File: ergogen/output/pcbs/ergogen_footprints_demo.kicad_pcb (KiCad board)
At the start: 2 copper layers, 95 x 95 mm, 53 parts

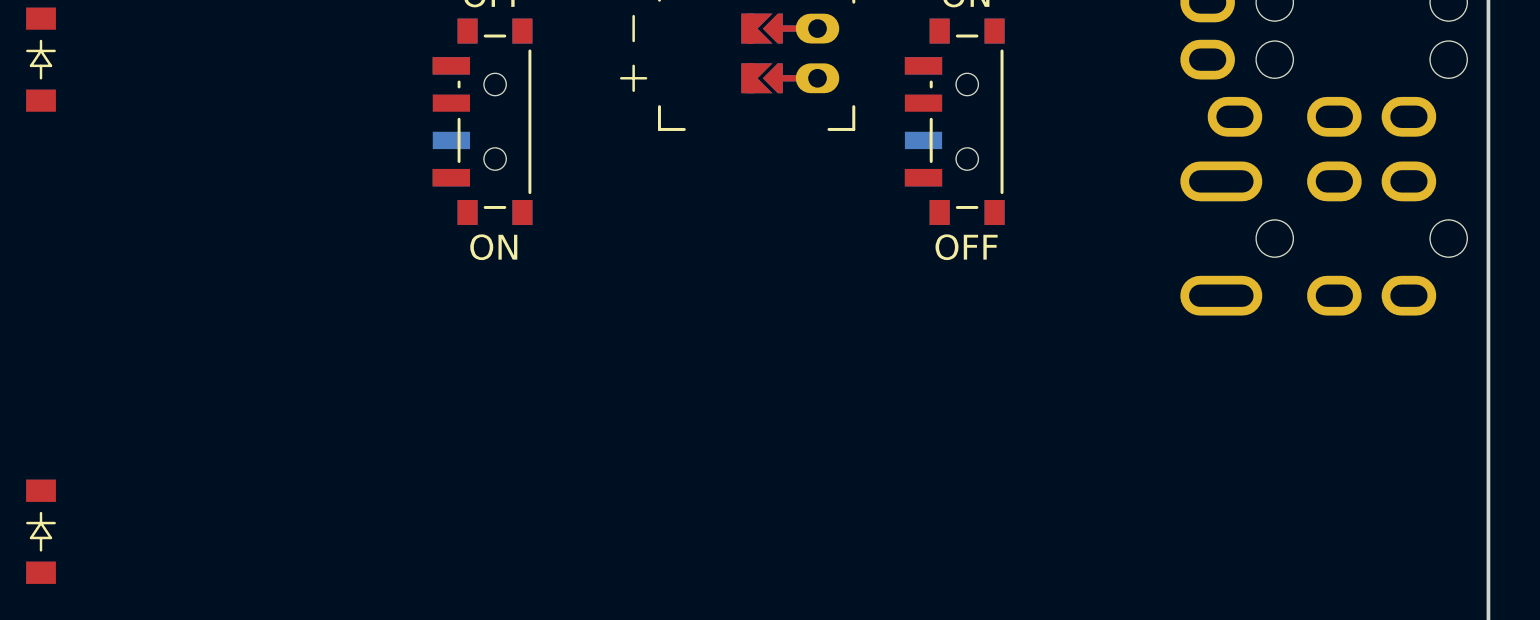
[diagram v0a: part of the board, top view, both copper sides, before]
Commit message: Add SSD1306 footprint
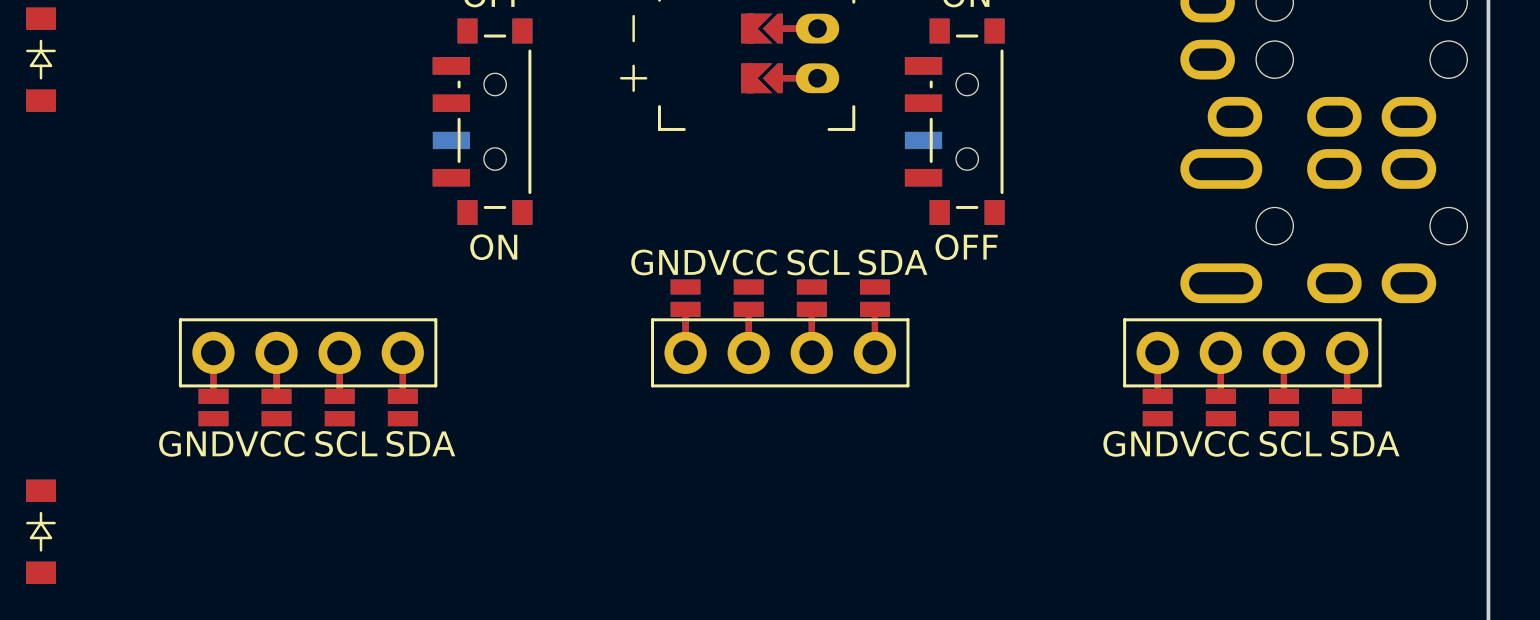
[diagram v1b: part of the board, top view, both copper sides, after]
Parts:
- added DISP4: , ceoloide:display_ssd1306, F.Cu at (138.0, 127.5)
- added DISP5: , ceoloide:display_ssd1306, F.Cu at (119.0, 127.5)
- added DISP6: , ceoloide:display_ssd1306, F.Cu at (100.0, 127.5)
- moved TRRS2 0.50 mm to (147.5, 108.0)
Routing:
- net VCC: track 7.51 -> 18.0 mm
- net SDA: track 10.5 -> 21.0 mm
- net SCL: track 10.5 -> 21.0 mm
- net GND: track 54.2 -> 64.7 mm

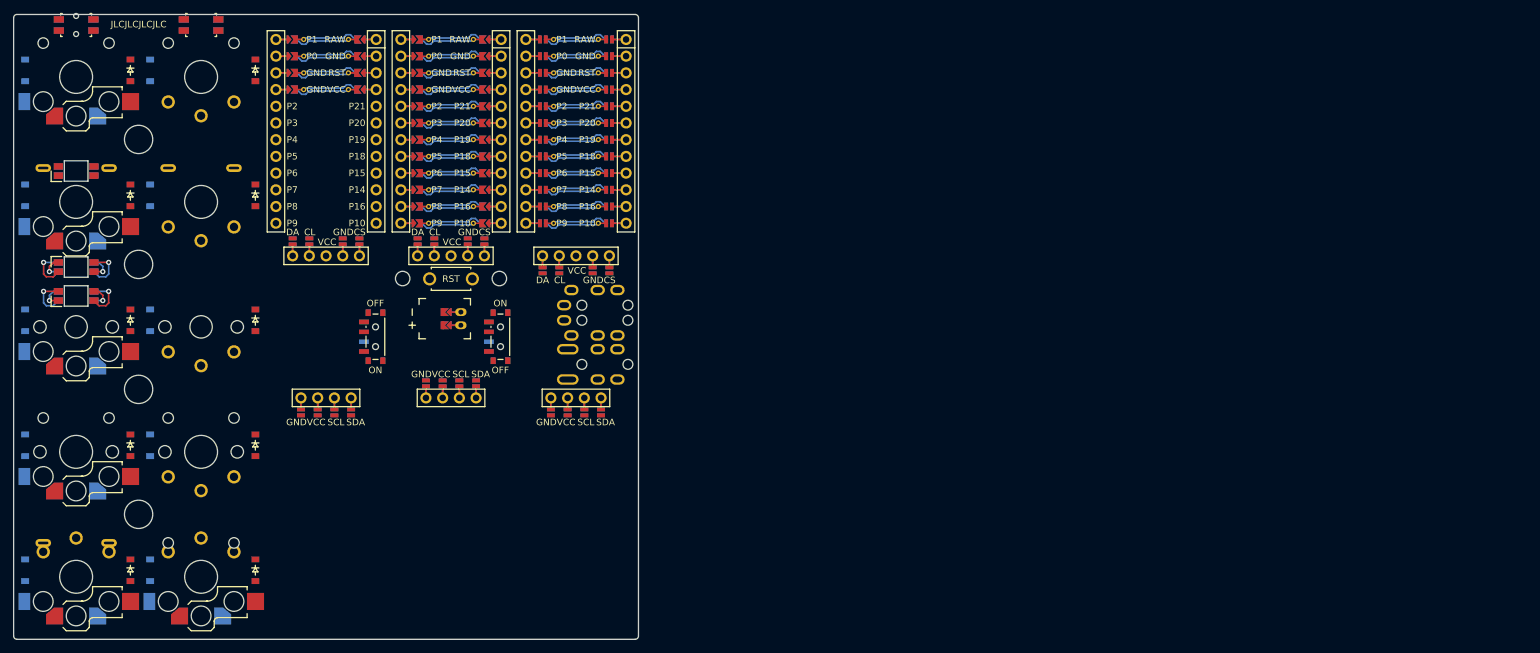
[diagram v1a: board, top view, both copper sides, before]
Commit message: Add mirror options to test footprints
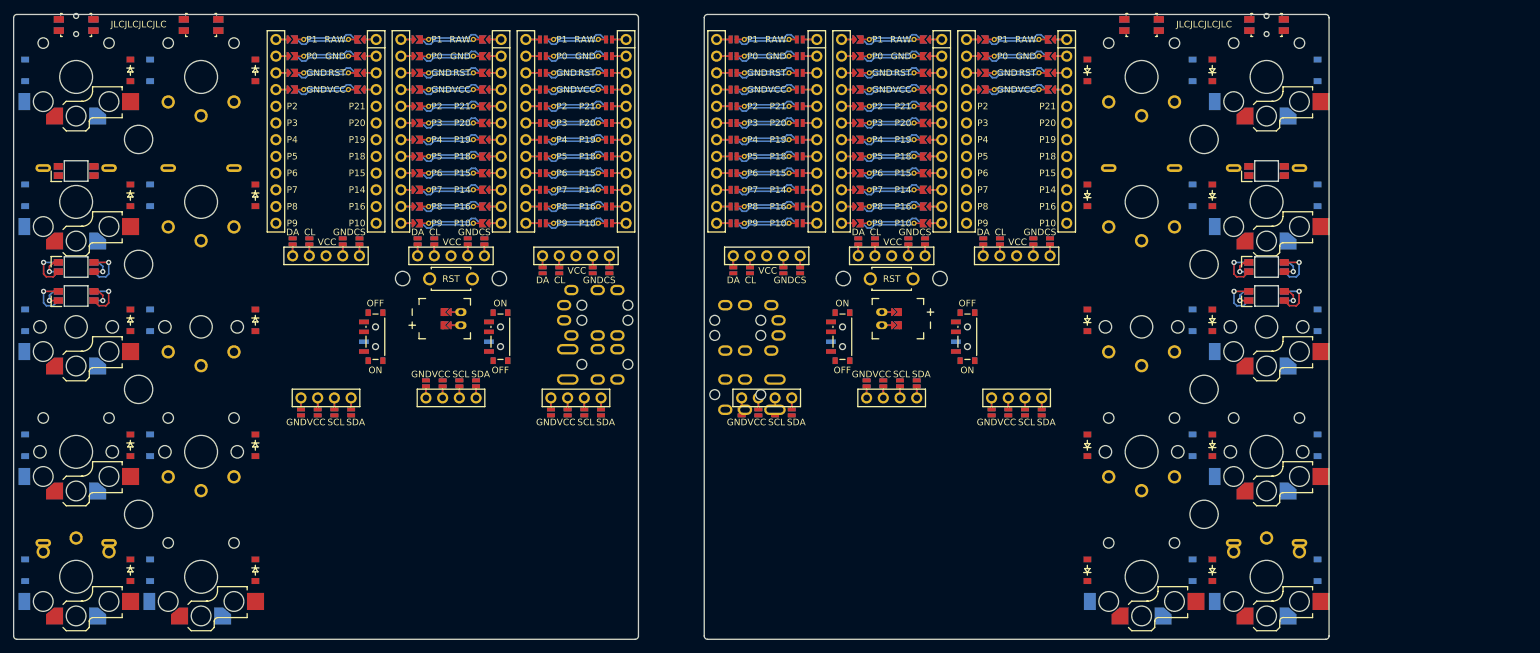
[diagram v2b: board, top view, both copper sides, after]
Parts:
- added D21: , ceoloide:diode_tht_sod123, F.Cu at (70.2, 137.0)
- added D22: , ceoloide:diode_tht_sod123, F.Cu at (70.2, 118.0)
- added D23: , ceoloide:diode_tht_sod123, F.Cu at (70.2, 99.0)
- added D24: , ceoloide:diode_tht_sod123, F.Cu at (70.2, 80.0)
- added D25: , ceoloide:diode_tht_sod123, F.Cu at (70.2, 61.0)
- added D26: , ceoloide:diode_tht_sod123, F.Cu at (89.2, 137.0)
- added D27: , ceoloide:diode_tht_sod123, F.Cu at (89.2, 118.0)
- added D28: , ceoloide:diode_tht_sod123, F.Cu at (89.2, 99.0)
- added D29: , ceoloide:diode_tht_sod123, F.Cu at (89.2, 80.0)
- added D30: , ceoloide:diode_tht_sod123, F.Cu at (89.2, 61.0)
- added D31: , ceoloide:diode_tht_sod123, F.Cu at (234.8, 137.0)
- added D32: , ceoloide:diode_tht_sod123, F.Cu at (234.8, 118.0)
- added D33: , ceoloide:diode_tht_sod123, F.Cu at (234.8, 99.0)
- added D34: , ceoloide:diode_tht_sod123, F.Cu at (234.8, 80.0)
- added D35: , ceoloide:diode_tht_sod123, F.Cu at (234.8, 61.0)
- added D36: , ceoloide:diode_tht_sod123, F.Cu at (215.8, 137.0)
- added D37: , ceoloide:diode_tht_sod123, F.Cu at (215.8, 118.0)
- added D38: , ceoloide:diode_tht_sod123, F.Cu at (215.8, 99.0)
- added D39: , ceoloide:diode_tht_sod123, F.Cu at (215.8, 80.0)
- added D40: , ceoloide:diode_tht_sod123, F.Cu at (215.8, 61.0)
- added DISP10: , ceoloide:display_ssd1306, F.Cu at (186.0, 127.5)
- added DISP11: , ceoloide:display_ssd1306, F.Cu at (100.0, 127.5)
- added DISP12: , ceoloide:display_ssd1306, F.Cu at (205.0, 127.5)
- added DISP7: , ceoloide:display_ssd1306, F.Cu at (138.0, 127.5)
- added DISP8: , ceoloide:display_ssd1306, F.Cu at (167.0, 127.5)
- added DISP9: , ceoloide:display_ssd1306, F.Cu at (119.0, 127.5)
- added JST2: , ceoloide/battery_connector_jst_ph_2, F.Cu at (184.5, 98.8)
- added LED4: , ceoloide:led_SK6812mini-e (per-key, reversible), B.Cu at (243.0, 95.3)
- added LED5: , ceoloide:led_SK6812mini-e (underglow, reversible), B.Cu at (62.0, 90.9)
- added LED6: , ceoloide:led_SK6812mini-e (underglow, reversible), B.Cu at (243.0, 90.9)
- added MCU4: , ceoloide:nice_nano, F.Cu at (186.0, 69.0)
- added MCU5: , ceoloide:nice_nano, F.Cu at (100.0, 69.0)
- added MCU6: , ceoloide:nice_nano, F.Cu at (205.0, 69.0)
- added MH10: , ceoloide:mounting_hole_npth, F.Cu at (193.3, 92.7)
- added MH11: , ceoloide:mounting_hole_npth, F.Cu at (126.3, 92.7)
- added MH12: , ceoloide:mounting_hole_npth, F.Cu at (178.7, 92.7)
- added MH7: , ceoloide:mounting_hole_npth, F.Cu at (233.5, 90.5)
- added MH8: , ceoloide:mounting_hole_npth, F.Cu at (233.5, 71.5)
- added MH9: , ceoloide:mounting_hole_npth, F.Cu at (111.7, 92.7)
- added PWR3: power_switch, ceoloide:power_switch_smd_side, F.Cu at (107.5, 101.5)
- added PWR4: power_switch, ceoloide:power_switch_smd_side, F.Cu at (197.5, 101.5)
- added RST4: reset_button_smd_side, ceoloide:reset_button_smd_side, F.Cu at (243.0, 54.1)
- added RST5: reset_switch_tht_top, ceoloide:reset_switch_tht_top, F.Cu at (119.0, 92.7)
- added RST6: reset_switch_tht_top, ceoloide:reset_switch_tht_top, F.Cu at (186.0, 92.7)
- added S11: , ceoloide:switch_choc_v1_v2, B.Cu at (81.0, 62.0)
- added S12: , ceoloide:switch_choc_v1_v2, B.Cu at (224.0, 62.0)
- added S13: , ceoloide:switch_choc_v1_v2, B.Cu at (81.0, 81.0)
- added S14: , ceoloide:switch_choc_v1_v2, B.Cu at (224.0, 81.0)
- added S15: , ceoloide:switch_choc_v1_v2, B.Cu at (81.0, 100.0)
- added S16: , ceoloide:switch_choc_v1_v2, B.Cu at (224.0, 100.0)
- added S17: , ceoloide:switch_choc_v1_v2, B.Cu at (81.0, 119.0)
- added S18: , ceoloide:switch_choc_v1_v2, B.Cu at (224.0, 119.0)
- added S19: , ceoloide:switch_choc_v1_v2, B.Cu at (81.0, 138.0)
- added S20: , ceoloide:switch_choc_v1_v2, B.Cu at (224.0, 138.0)
- added TRRS3: TRRS-PJ-320A-dual, ceoloide:trrs_pj320a (reversible, symmetric), F.Cu at (147.5, 108.0)
- added TRRS4: TRRS-PJ-320A-dual, ceoloide:trrs_pj320a (reversible, symmetric), F.Cu at (157.5, 108.0)
- D11, D12, D13, D14, D15, D16, D17, D18, D19, D20: moved to B.Cu
- DISP4, DISP5, DISP6: footprint ceoloide:display_ssd1306 -> ceoloide:nice_view
- LED3: footprint ceoloide:led_SK6812mini-e (underglow, reversible) -> ceoloide:led_SK6812mini-e (per-key, reversible)
- RST3: value reset_switch_tht_top -> reset_button_smd_side; footprint ceoloide:reset_switch_tht_top -> ceoloide:reset_button_smd_side
- TRRS2: footprint ceoloide:trrs_pj320a (reversible, symmetric) -> ceoloide:trrs_pj320a (reversible)
- moved S4 184.9 mm to (243.0, 81.0)
- moved LED2 182.0 mm to (243.0, 76.3)
- moved S2 182.0 mm to (243.0, 62.0)
- moved D11 180.5 mm to (250.8, 137.0), turned to 90 degrees
- moved D12 180.5 mm to (250.8, 118.0), turned to 90 degrees
- moved D13 180.5 mm to (250.8, 99.0), turned to 90 degrees
- moved D14 180.5 mm to (250.8, 80.0), turned to 90 degrees
- moved D15 180.5 mm to (250.8, 61.0), turned to 90 degrees
- moved S6 166.4 mm to (243.0, 100.0)
- moved S8 163.1 mm to (243.0, 119.0)
- moved RST2 162.0 mm to (224.0, 54.1)
- moved S10 162.0 mm to (243.0, 138.0)
- moved D16 142.5 mm to (231.8, 137.0), turned to 90 degrees
- moved D17 142.5 mm to (231.8, 118.0), turned to 90 degrees
- moved D18 142.5 mm to (231.8, 99.0), turned to 90 degrees
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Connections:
- D11 pad 2: c1_r5 -> mirror_c1_r5
- D12 pad 2: c1_r4 -> mirror_c1_r4
- D13 pad 2: c1_r3 -> mirror_c1_r3
- D14 pad 2: c1_r2 -> mirror_c1_r2
- D15 pad 2: c1_r1 -> mirror_c1_r1
- D16 pad 2: c2_r5 -> mirror_c2_r5
- D17 pad 2: c2_r4 -> mirror_c2_r4
- D18 pad 2: c2_r3 -> mirror_c2_r3
- D19 pad 2: c2_r2 -> mirror_c2_r2
- D20 pad 2: c2_r1 -> mirror_c2_r1
- DISP2 pad 10: DISP2_1 -> CS
- DISP2 pad 11: DISP2_2 -> GND
- DISP2 pad 12: DISP2_4 -> SCL
- DISP2 pad 13: DISP2_5 -> SDA
- DISP2 pad 14: CS -> DISP2_1
- DISP2 pad 15: GND -> DISP2_2
- DISP2 pad 16: SCL -> DISP2_4
- DISP2 pad 17: SDA -> DISP2_5
- DISP2 pad 20: DISP2_5 -> CS
- DISP2 pad 21: DISP2_4 -> GND
- DISP2 pad 22: DISP2_2 -> SCL
- DISP2 pad 23: DISP2_1 -> SDA
- DISP2 pad 24: CS -> DISP2_5
- DISP2 pad 25: GND -> DISP2_4
- DISP2 pad 26: SCL -> DISP2_2
- DISP2 pad 27: SDA -> DISP2_1
- DISP4 pad 12: DISP4_3 -> DISP4_4
- DISP4 pad 13: DISP4_4 -> DISP4_5
- DISP4 pad 14: GND -> CS
- DISP4 pad 15: VCC -> GND
- DISP4 pad 20: DISP4_4 -> DISP4_5
- DISP4 pad 21: DISP4_3 -> DISP4_4
- DISP4 pad 24: GND -> CS
- DISP4 pad 25: VCC -> GND
- DISP4 pad 3: DISP4_3 -> VCC
- DISP5 pad 10: GND -> DISP5_1
- DISP5 pad 11: VCC -> DISP5_2
- DISP5 pad 12: SCL -> DISP5_4
- DISP5 pad 13: SDA -> DISP5_5
- DISP5 pad 14: DISP5_1 -> CS
- DISP5 pad 15: DISP5_2 -> GND
- DISP5 pad 16: DISP5_3 -> SCL
- DISP5 pad 17: DISP5_4 -> SDA
- DISP5 pad 20: GND -> DISP5_5
- DISP5 pad 21: VCC -> DISP5_4
- DISP5 pad 22: SCL -> DISP5_2
- DISP5 pad 23: SDA -> DISP5_1
- DISP5 pad 24: DISP5_4 -> CS
- DISP5 pad 25: DISP5_3 -> GND
- DISP5 pad 26: DISP5_2 -> SCL
- DISP5 pad 27: DISP5_1 -> SDA
- DISP5 pad 3: DISP5_3 -> VCC
- DISP6 pad 12: DISP6_3 -> DISP6_4
- DISP6 pad 13: DISP6_4 -> DISP6_5
- DISP6 pad 14: GND -> CS
- DISP6 pad 15: VCC -> GND
- DISP6 pad 20: DISP6_4 -> DISP6_5
- DISP6 pad 21: DISP6_3 -> DISP6_4
- DISP6 pad 24: GND -> CS
- DISP6 pad 25: VCC -> GND
- DISP6 pad 3: DISP6_3 -> VCC
- LED2 pad 2: LED_3 -> LED_U_1
- LED2 pad 4: LED_2 -> LED
- LED3 pad 2: LED_2 -> LED_3
- LED3 pad 4: LED_U_1 -> LED_2
- MCU2 pad 1: MCU2_1 -> RAW
- MCU2 pad 10: MCU2_10 -> P14
- MCU2 pad 11: MCU2_11 -> P16
- MCU2 pad 12: MCU2_12 -> P10
- MCU2 pad 13: MCU2_13 -> MCU2_12
- MCU2 pad 14: MCU2_14 -> MCU2_11
- MCU2 pad 15: MCU2_15 -> MCU2_10
- MCU2 pad 16: MCU2_16 -> MCU2_9
- MCU2 pad 17: MCU2_17 -> MCU2_8
- MCU2 pad 18: MCU2_18 -> MCU2_7
- MCU2 pad 19: MCU2_19 -> MCU2_6
- MCU2 pad 2: MCU2_2 -> GND
- MCU2 pad 20: MCU2_20 -> MCU2_5
- MCU2 pad 21: MCU2_21 -> MCU2_4
- MCU2 pad 22: MCU2_22 -> MCU2_3
- MCU2 pad 23: MCU2_23 -> MCU2_2
- MCU2 pad 24: MCU2_24 -> MCU2_1
- MCU2 pad 3: MCU2_3 -> RST
- MCU2 pad 4: MCU2_4 -> VCC
- MCU2 pad 5: MCU2_5 -> P21
- MCU2 pad 6: MCU2_6 -> P20
- MCU2 pad 7: MCU2_7 -> P19
- MCU2 pad 8: MCU2_8 -> P18
- MCU2 pad 9: MCU2_9 -> P15
- MCU3 pad 10: P14 -> MCU3_10
- MCU3 pad 11: P16 -> MCU3_11
- MCU3 pad 12: P10 -> MCU3_12
- MCU3 pad 13: P9 -> MCU3_13
- MCU3 pad 14: P8 -> MCU3_14
- MCU3 pad 15: P7 -> MCU3_15
- MCU3 pad 16: P6 -> MCU3_16
- MCU3 pad 17: P5 -> MCU3_17
- MCU3 pad 18: P4 -> MCU3_18
- MCU3 pad 19: P3 -> MCU3_19
- MCU3 pad 20: P2 -> MCU3_20
- MCU3 pad 5: P21 -> MCU3_5
- MCU3 pad 6: P20 -> MCU3_6
- MCU3 pad 7: P19 -> MCU3_7
- MCU3 pad 8: P18 -> MCU3_8
- MCU3 pad 9: P15 -> MCU3_9
- RST3 pad 1: RST -> GND
- RST3 pad 2: GND -> RST
- S10 pad : c2_r5 -> mirror_c1_r5
- S10 pad 1: c2_r5 -> mirror_c1_r5
- S2 pad 2: c1_r2 -> mirror_c1_r1
- S3 pad 2: c1_r3 -> c1_r2
- S4 pad 2: c1_r4 -> mirror_c1_r2
- S5 pad : c1_r5 -> (no net)
- S5 pad 1: c1_r5 -> (no net)
- S5 pad 2: (no net) -> c1_r3
- S6 pad 1: c2_r1 -> (no net)
- S6 pad 2: (no net) -> mirror_c1_r3
- S7 pad 1: c2_r2 -> (no net)
- S7 pad 2: (no net) -> c1_r4
- S8 pad 1: c2_r3 -> (no net)
- S8 pad 2: (no net) -> mirror_c1_r4
- S9 pad : (no net) -> c1_r5
- S9 pad 1: c2_r4 -> c1_r5
- TRRS2 pad 2: GND -> B
- TRRS2 pad 3: VCC -> GND
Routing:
- net mirror_c2_r5: track 0.00 -> 474.0 mm
- net mirror_c1_r1: track 0.00 -> 473.2 mm
- net LED: track 0.00 -> 237.4 mm
- net P20: track 237.0 -> 0.00 mm
- net c1_r2: track 236.6 -> 0.00 mm
- net GND: track 64.7 -> 294.5 mm, vias 2 -> 4
- net P15: track 118.7 -> 0.00 mm
- net P14: track 118.7 -> 0.00 mm
- net c2_r2: track 0.00 -> 72.3 mm
- net c1_r1: track 36.2 -> 72.3 mm
- net SDA: track 21.0 -> 42.0 mm
- net SCL: track 21.0 -> 42.0 mm
- net VCC: track 18.0 -> 36.0 mm, vias 2 -> 4
- net LED_2: track 13.5 -> 27.1 mm, vias 2 -> 4
- net CS: track 10.5 -> 21.0 mm
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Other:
- board size 95 x 95 mm -> 200 x 95 mm

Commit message: Add `resist` on diodes to keep them asymmetric
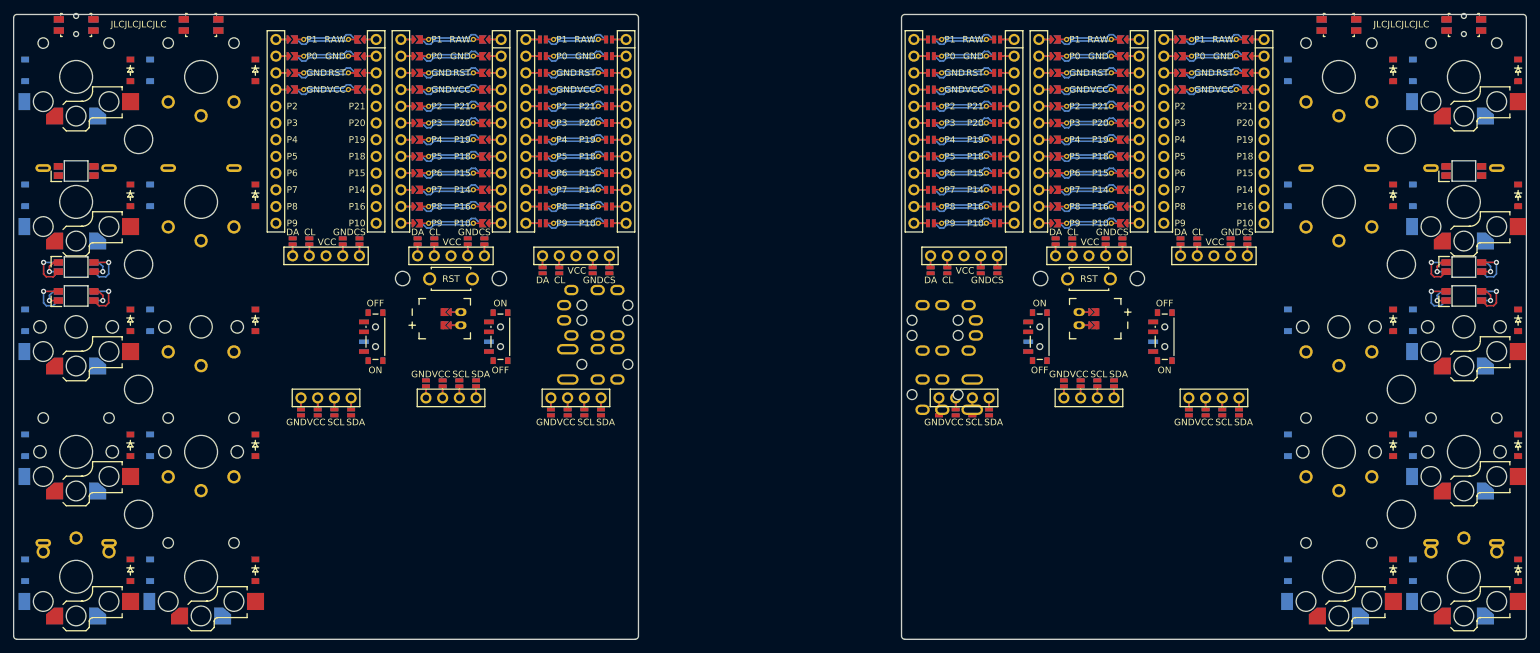
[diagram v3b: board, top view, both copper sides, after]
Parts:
- moved D31 46.5 mm to (281.2, 137.0), turned to -90 degrees
- moved D32 46.5 mm to (281.2, 118.0), turned to -90 degrees
- moved D33 46.5 mm to (281.2, 99.0), turned to -90 degrees
- moved D34 46.5 mm to (281.2, 80.0), turned to -90 degrees
- moved D35 46.5 mm to (281.2, 61.0), turned to -90 degrees
- moved D36 46.5 mm to (262.2, 137.0), turned to -90 degrees
- moved D37 46.5 mm to (262.2, 118.0), turned to -90 degrees
- moved D38 46.5 mm to (262.2, 99.0), turned to -90 degrees
- moved D39 46.5 mm to (262.2, 80.0), turned to -90 degrees
- moved D40 46.5 mm to (262.2, 61.0), turned to -90 degrees
- moved DISP10 30.0 mm to (216.0, 127.5)
- moved DISP12 30.0 mm to (235.0, 127.5)
- moved DISP2 30.0 mm to (197.0, 72.5)
- moved DISP4 30.0 mm to (216.0, 72.5)
- moved DISP6 30.0 mm to (235.0, 72.5)
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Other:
- board size 200 x 95 mm -> 230 x 95 mm

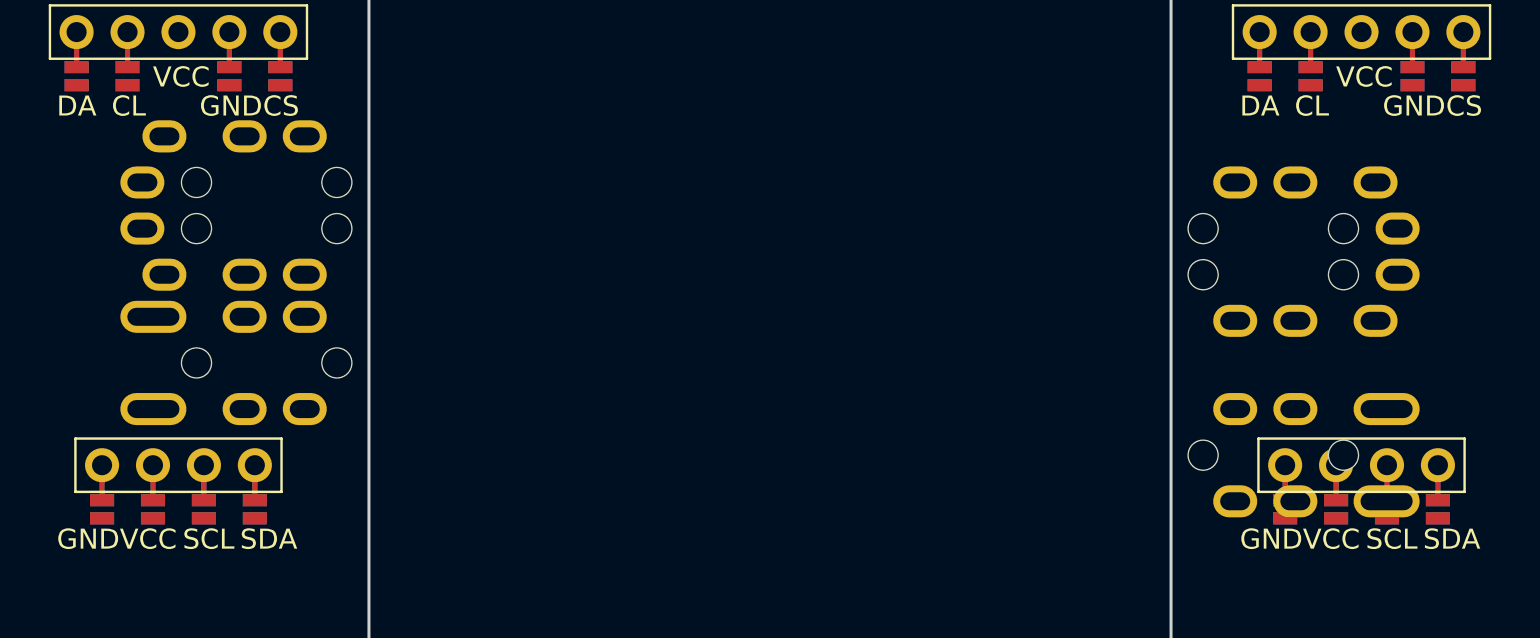
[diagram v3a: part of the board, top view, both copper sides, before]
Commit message: Update TRRS positions and related footprint library
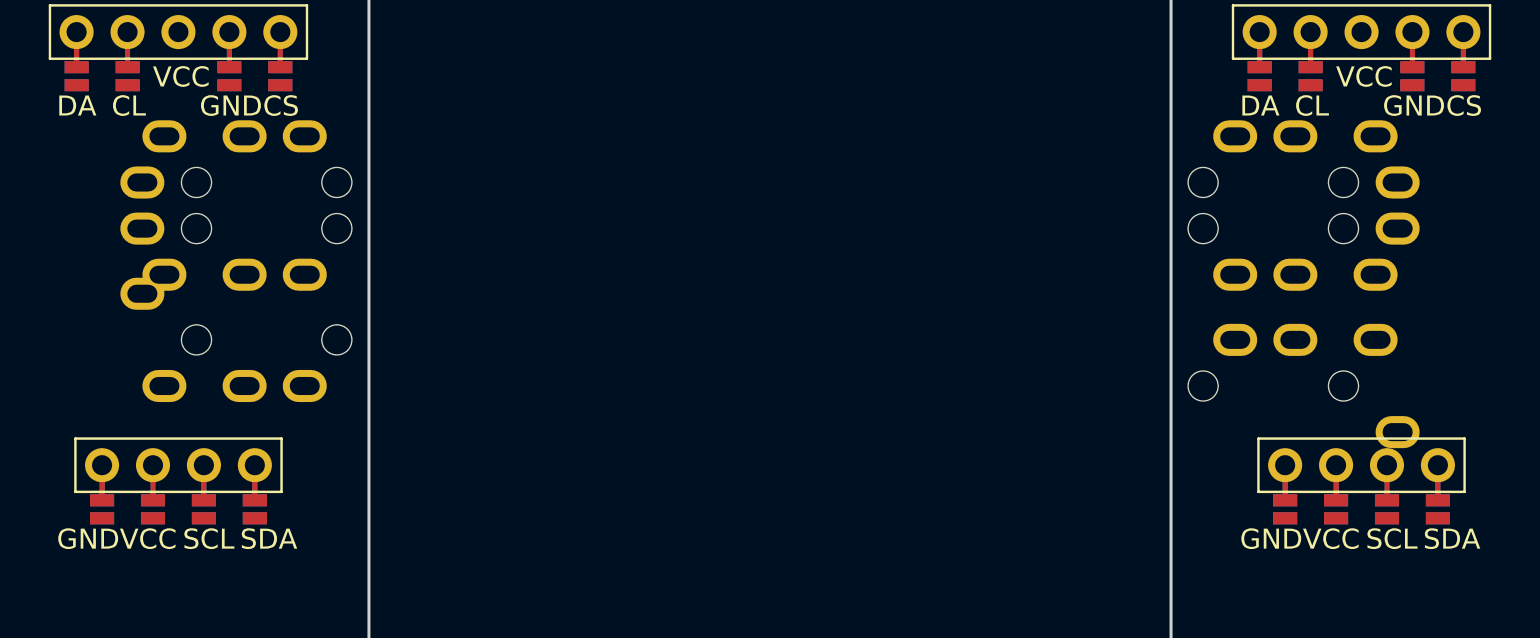
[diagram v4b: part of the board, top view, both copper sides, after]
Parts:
- TRRS3, TRRS4: footprint ceoloide:trrs_pj320a (reversible, symmetric) -> ceoloide:trrs_pj320a
- moved TRRS3 2.30 mm to (147.5, 105.7)
- moved TRRS4 2.30 mm to (187.5, 105.7)
- moved TRRS1 1.15 mm to (147.5, 97.8)
- moved TRRS2 1.15 mm to (187.5, 97.8)
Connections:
- TRRS3 pad 2: GND -> B
- TRRS3 pad 3: VCC -> GND
- TRRS4 pad 2: GND -> B
- TRRS4 pad 3: VCC -> GND
